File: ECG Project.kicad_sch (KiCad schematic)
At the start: 12 parts, among them J1 Battery, J2 Conn_01x03_Pin, U1 AD620, U2 ${SIM.PARAMS}, U3 ${SIM.PARAMS}

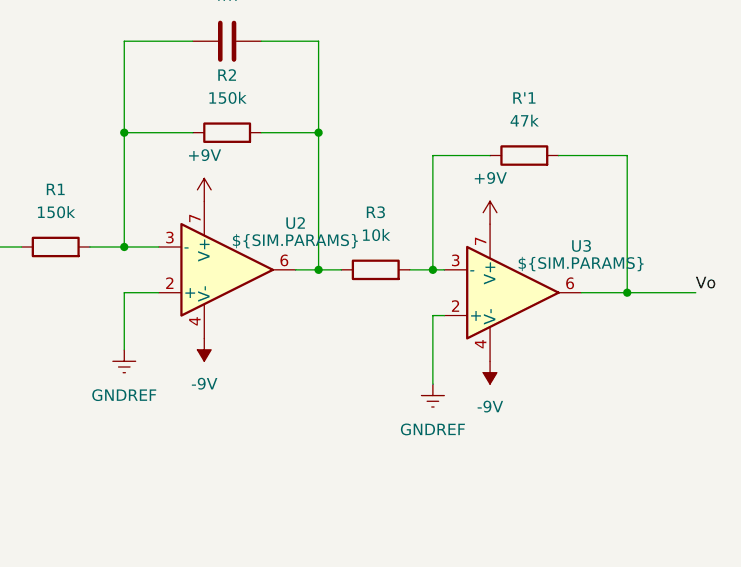
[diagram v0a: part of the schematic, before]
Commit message: Update U2-3 pinout
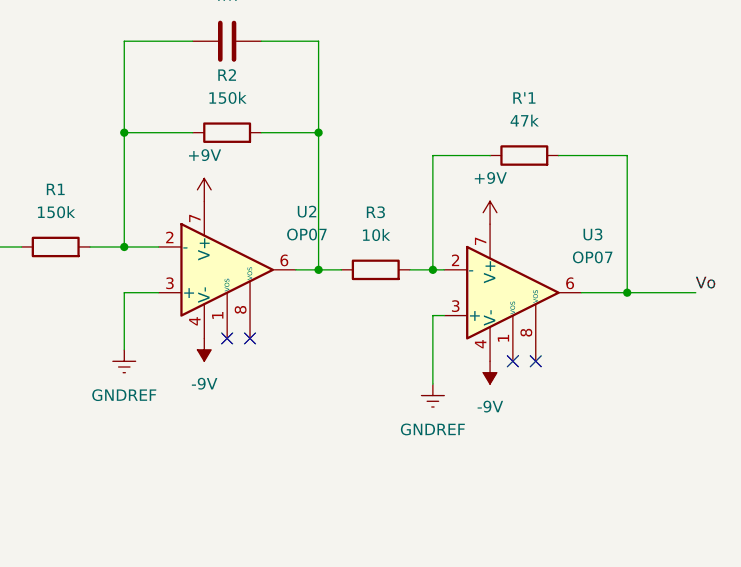
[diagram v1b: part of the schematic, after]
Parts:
- removed U2, U3: ${SIM.PARAMS}, Package_DIP:DIP-8_W7.62mm, symbol Simulation_SPICE:OPAMP
- added U2, U3: OP07, Package_DIP:DIP-8_W7.62mm, symbol Amplifier_Operational:OP07
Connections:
- net +9V: now also U2.7 (V+), U3.7 (V+)
- net -9V: now also U2.4 (V-), U3.4 (V-)
- net GNDREF: now also U2.3 (+), U3.3 (+)
- net Vo: now also U3.6
- net at Cf1.1, R1.2, R2.1: now also U2.2 (-)
- net at Cf1.2, R2.2, R3.1: now also U2.6
- net at R'1.1, R3.2: now also U3.2 (-)
- no-connect marks 0 -> 4
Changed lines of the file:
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@@
 		(color 0 0 0 0)
+	)
+	(no_connect
+		(at 114.3 110.49)
+	)
+	(no_connect
+		(at 148.59 113.03)
+	)
+	(no_connect
+		(at 146.05 113.03)
+	)
+	(no_connect
+		(at 116.84 110.49)
 	)
 	(wire
@@
 	)
 	(symbol
+		(lib_name "OP07_1")
+		(lib_id "Amplifier_Operational:OP07")
+		(at 146.05 105.41 0)
+		(unit 1)
+		(body_style 1)
+		(exclude_from_sim no)
+		(in_bom yes)
+		(on_board yes)
+		(in_pos_files yes)
+		(dnp no)
+		(fields_autoplaced yes)
+		(property "Reference" "U3"
+			(at 154.94 98.9898 0)
+			(show_name no)
+			(do_not_autoplace no)
+			(effects
+				(font
+					(size 1.27 1.27)
+				)
+			)
+		)
+		(property "Value" "OP07"
+			(at 154.94 101.5298 0)
+			(show_name no)
+			(do_not_autoplace no)
+			(effects
+				(font
+					(size 1.27 1.27)
+				)
+			)
+		)
+		(property "Footprint" "Package_DIP:DIP-8_W7.62mm"
+			(at 147.32 104.14 0)
+			(hide yes)
+			(show_name no)
+			(do_not_autoplace no)
+			(effects
+				(font
+					(size 1.27 1.27)
+				)
+			)
+		)
+		(property "Datasheet" "https://www.analog.com/media/en/technical-documentation/data-sheets/OP07.pdf"
+			(at 147.32 101.6 0)
+			(hide yes)
+			(show_name no)
+			(do_not_autoplace no)
+			(effects
+				(font
+					(size 1.27 1.27)
+				)
+			)
+		)
+		(property "Description" "Single Ultra-Low Offset Voltage Operational Amplifier, DIP-8/SOIC-8"
+			(at 146.05 105.41 0)
+			(hide yes)
+			(show_name no)
+			(do_not_autoplace no)
+			(effects
+				(font
+					(size 1.27 1.27)
+				)
+			)
+		)
+		(pin "8"
+		)
+		(pin "5"
+		)
+		(pin "7"
+		)
+		(pin "4"
+		)
+		(pin "3"
+		)
+		(pin "2"
+		)
+		(pin "1"
+		)
+		(pin "6"
+		)
+		(instances
+			(project "ECG Project"
+				(path "/b25dd311-7505-49a1-85e7-a6d1ec80d902"
+					(reference "U3")
+					(unit 1)
+				)
+			)
+		)
+	)
+	(symbol
 		(lib_id "Amplifier_Instrumentation:AD620")
 		(at 60.96 100.33 0)
@@
 	)
 	(symbol
+		(lib_name "OP07_1")
+		(lib_id "Amplifier_Operational:OP07")
+		(at 114.3 102.87 0)
+		(unit 1)
+		(body_style 1)
+		(exclude_from_sim no)
+		(in_bom yes)
+		(on_board yes)
+		(in_pos_files yes)
+		(dnp no)
+		(fields_autoplaced yes)
+		(property "Reference" "U2"
+			(at 123.19 96.4498 0)
+			(show_name no)
+			(do_not_autoplace no)
+			(effects
+				(font
+					(size 1.27 1.27)
+				)
+			)
+		)
+		(property "Value" "OP07"
+			(at 123.19 98.9898 0)
+			(show_name no)
+			(do_not_autoplace no)
+			(effects
+				(font
+					(size 1.27 1.27)
+				)
+			)
+		)
+		(property "Footprint" "Package_DIP:DIP-8_W7.62mm"
+			(at 115.57 101.6 0)
+			(hide yes)
+			(show_name no)
+			(do_not_autoplace no)
+			(effects
+				(font
+					(size 1.27 1.27)
+				)
+			)
+		)
+		(property "Datasheet" "https://www.analog.com/media/en/technical-documentation/data-sheets/OP07.pdf"
+			(at 115.57 99.06 0)
+			(hide yes)
+			(show_name no)
+			(do_not_autoplace no)
+			(effects
+				(font
+					(size 1.27 1.27)
+				)
+			)
+		)
+		(property "Description" "Single Ultra-Low Offset Voltage Operational Amplifier, DIP-8/SOIC-8"
+			(at 114.3 102.87 0)
+			(hide yes)
+			(show_name no)
+			(do_not_autoplace no)
+			(effects
+				(font
+					(size 1.27 1.27)
+				)
+			)
+		)
+		(pin "8"
+		)
+		(pin "5"
+		)
+		(pin "7"
+		)
+		(pin "4"
+		)
+		(pin "3"
+		)
+		(pin "2"
+		)
+		(pin "1"
+		)
+		(pin "6"
+		)
+		(instances
+			(project "ECG Project"
+				(path "/b25dd311-7505-49a1-85e7-a6d1ec80d902"
+					(reference "U2")
+					(unit 1)
+				)
+			)
+		)
+	)
+	(symbol
 		(lib_id "Device:C")
 		(at 114.3 77.47 90)
@@
 	)
 	(symbol
-		(lib_name "OPAMP_2")
-		(lib_id "Simulation_SPICE:OPAMP")
-		(at 146.05 105.41 0)
-		(unit 1)
-		(body_style 1)
-		(exclude_from_sim no)
-		(in_bom yes)
-		(on_board yes)
-		(in_pos_files yes)
-		(dnp no)
-		(property "Reference" "U3"
-			(at 153.67 100.2598 0)
-			(show_name no)
-			(do_not_autoplace no)
-			(effects
-				(font
-					(size 1.27 1.27)
-				)
-			)
-		)
-		(property "Value" "${SIM.PARAMS}"
-			(at 153.67 102.1649 0)
-			(show_name no)
-			(do_not_autoplace no)
-			(effects
-				(font
-					(size 1.27 1.27)
-				)
-			)
-		)
-		(property "Footprint" "Package_DIP:DIP-8_W7.62mm"
-			(at 146.05 105.41 0)
-			(hide yes)
-			(show_name no)
-			(do_not_autoplace no)
-			(effects
-				(font
-					(size 1.27 1.27)
-				)
-			)
-		)
-		(property "Datasheet" "https://ngspice.sourceforge.io/docs/ngspice-html-manual/manual.xhtml#sec__SUBCKT_Subcircuits"
-			(at 146.05 105.41 0)
-			(hide yes)
-			(show_name no)
-			(do_not_autoplace no)
-			(effects
-				(font
-					(size 1.27 1.27)
-				)
-			)
-		)
-		(property "Description" "Operational amplifier, single"
-			(at 146.05 105.41 0)
-			(hide yes)
-			(show_name no)
-			(do_not_autoplace no)
-			(effects
-				(font
-					(size 1.27 1.27)
-				)
-			)
-		)
-		(property "Sim.Pins" "1=in+ 2=in- 3=vcc 4=vee 5=out"
-			(at 146.05 105.41 0)
-			(hide yes)
-			(show_name no)
-			(do_not_autoplace no)
-			(effects
-				(font
-					(size 1.27 1.27)
-				)
-			)
-		)
-		(property "Sim.Device" "SUBCKT"
-			(at 146.05 105.41 0)
-			(hide yes)
-			(show_name no)
-			(do_not_autoplace no)
-			(effects
-				(font
-					(size 1.27 1.27)
-				)
-				(justify left)
-			)
-		)
-		(property "Sim.Library" "${KICAD9_SYMBOL_DIR}/Simulation_SPICE.sp"
-			(at 146.05 105.41 0)
-			(hide yes)
-			(show_name no)
-			(do_not_autoplace no)
-			(effects
-				(font
-					(size 1.27 1.27)
-				)
-			)
-		)
-		(property "Sim.Name" "kicad_builtin_opamp"
-			(at 146.05 105.41 0)
-			(hide yes)
-			(show_name no)
-			(do_not_autoplace no)
-			(effects
-				(font
-					(size 1.27 1.27)
-				)
-			)
-		)
-		(pin "6"
-		)
-		(pin "2"
-		)
-		(pin "7"
-		)
-		(pin "4"
-		)
-		(pin "3"
-		)
-		(instances
-			(project "ECG Project"
-				(path "/b25dd311-7505-49a1-85e7-a6d1ec80d902"
-					(reference "U3")
-					(unit 1)
-				)
-			)
-		)
-	)
-	(symbol
 		(lib_id "Device:R")
 		(at 147.32 90.17 90)
@@
 					(unit 1)
 				)
-			)
-		)
-	)
-	(symbol
-		(lib_name "OPAMP_1")
-		(lib_id "Simulation_SPICE:OPAMP")
-		(at 114.3 102.87 0)
-		(unit 1)
-		(body_style 1)
-		(exclude_from_sim no)
-		(in_bom yes)
-		(on_board yes)
-		(in_pos_files yes)
-		(dnp no)
-		(property "Reference" "U2"
-			(at 121.92 97.7198 0)
-			(show_name no)
-			(do_not_autoplace no)
-			(effects
-				(font
-					(size 1.27 1.27)
-				)
-			)
-		)
-		(property "Value" "${SIM.PARAMS}"
-			(at 121.92 99.6249 0)
-			(show_name no)
-			(do_not_autoplace no)
-			(effects
-				(font
-					(size 1.27 1.27)
-				)
-			)
-		)
-		(property "Footprint" "Package_DIP:DIP-8_W7.62mm"
-			(at 114.3 102.87 0)
-			(hide yes)
-			(show_name no)
-			(do_not_autoplace no)
-			(effects
-				(font
-					(size 1.27 1.27)
-				)
-			)
-		)
-		(property "Datasheet" "https://ngspice.sourceforge.io/docs/ngspice-html-manual/manual.xhtml#sec__SUBCKT_Subcircuits"
-			(at 114.3 102.87 0)
-			(hide yes)
-			(show_name no)
-			(do_not_autoplace no)
-			(effects
-				(font
-					(size 1.27 1.27)
-				)
-			)
-		)
-		(property "Description" "Operational amplifier, single"
-			(at 114.3 102.87 0)
-			(hide yes)
-			(show_name no)
-			(do_not_autoplace no)
-			(effects
-				(font
-					(size 1.27 1.27)
-				)
-			)
-		)
-		(property "Sim.Pins" "1=in+ 2=in- 3=vcc 4=vee 5=out"
-			(at 114.3 102.87 0)
-			(hide yes)
-			(show_name no)
-			(do_not_autoplace no)
-			(effects
-				(font
-					(size 1.27 1.27)
-				)
-			)
-		)
-		(property "Sim.Device" "SUBCKT"
-			(at 114.3 102.87 0)
-			(hide yes)
-			(show_name no)
-			(do_not_autoplace no)
-			(effects
-				(font
-					(size 1.27 1.27)
-				)
-				(justify left)
-			)
-		)
-		(property "Sim.Library" "${KICAD9_SYMBOL_DIR}/Simulation_SPICE.sp"
-			(at 114.3 102.87 0)
-			(hide yes)
-			(show_name no)
-			(do_not_autoplace no)
-			(effects
-				(font
-					(size 1.27 1.27)
-				)
-			)
-		)
-		(property "Sim.Name" "kicad_builtin_opamp"
-			(at 114.3 102.87 0)
-			(hide yes)
-			(show_name no)
-			(do_not_autoplace no)
-			(effects
-				(font
-					(size 1.27 1.27)
-				)
-			)
-		)
-		(pin "6"
-		)
-		(pin "2"
-		)
-		(pin "7"
-		)
-		(pin "4"
-		)
-		(pin "3"
-		)
-		(instances
-			(project "ECG Project"
-				(path "/b25dd311-7505-49a1-85e7-a6d1ec80d902"
-					(reference "U2")
-					(unit 1)
-				)

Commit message: Changed capacitor sizes
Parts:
- Cf1: footprint Capacitor_THT:C_Radial_D5.0mm_H11.0mm_P2.00mm -> Capacitor_THT:C_Disc_D4.7mm_W2.5mm_P5.00mm
- Ci1: footprint Capacitor_THT:C_Radial_D5.0mm_H11.0mm_P2.00mm -> Capacitor_THT:C_Radial_D8.0mm_H11.5mm_P3.50mm
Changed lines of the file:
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@@
 			)
 		)
-		(property "Footprint" "Capacitor_THT:C_Radial_D5.0mm_H11.0mm_P2.00mm"
+		(property "Footprint" "Capacitor_THT:C_Disc_D4.7mm_W2.5mm_P5.00mm"
 			(at 118.11 76.5048 0)
 			(hide yes)
@@
 			)
 		)
-		(property "Footprint" "Capacitor_THT:C_Radial_D5.0mm_H11.0mm_P2.00mm"
+		(property "Footprint" "Capacitor_THT:C_Radial_D8.0mm_H11.5mm_P3.50mm"
 			(at 87.63 99.3648 0)
 			(hide yes)
